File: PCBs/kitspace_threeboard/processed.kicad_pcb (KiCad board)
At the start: 2 copper layers, 58.2 x 49.3 mm, 52 parts, among them J1 USB_mini_micro_B, K1 KEYSW, K2 KEYSW, K3 KEYSW, SW1 SW_PUSH, U1 ATMEGA32U4, U2 24LC512, U3 24LC512, X1 XTAL_GND

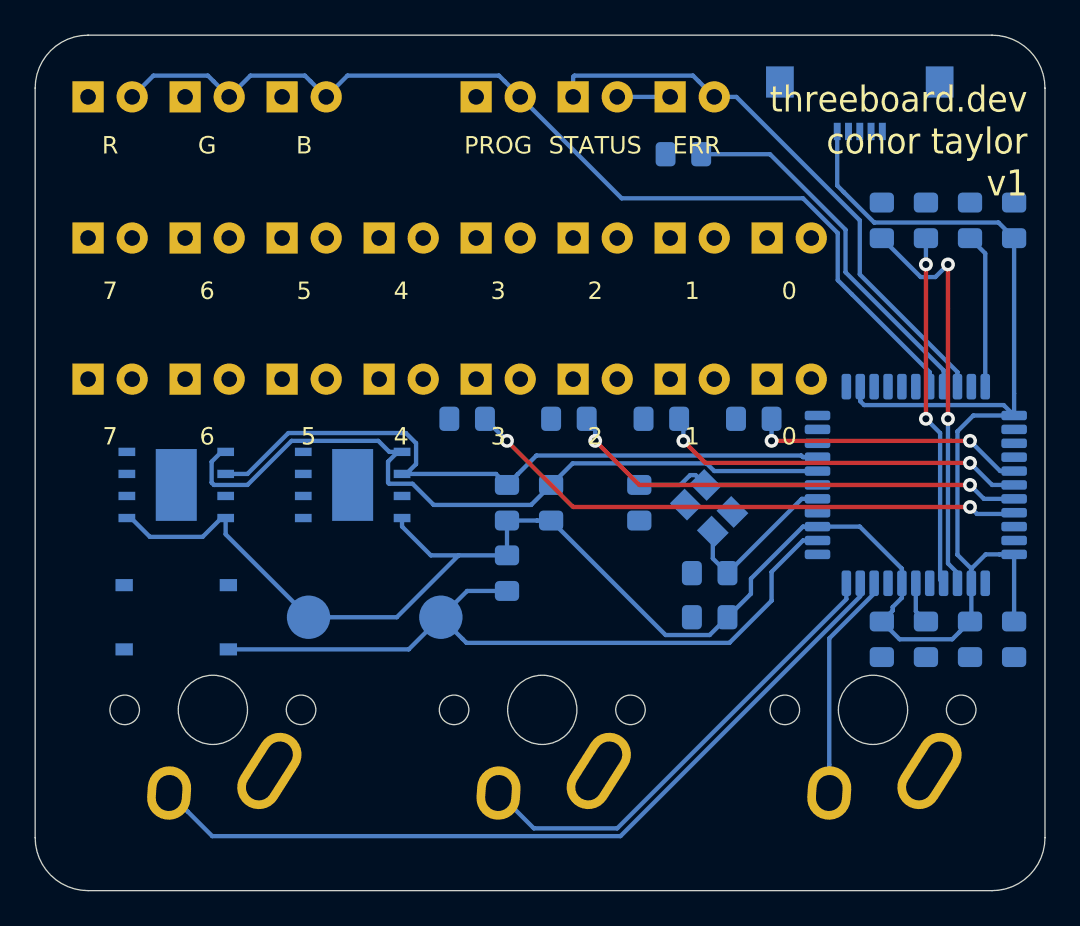
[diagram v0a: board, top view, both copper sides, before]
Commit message: recheck all circuits and clean up fill zone by rerouting the nets using freerouting and manually
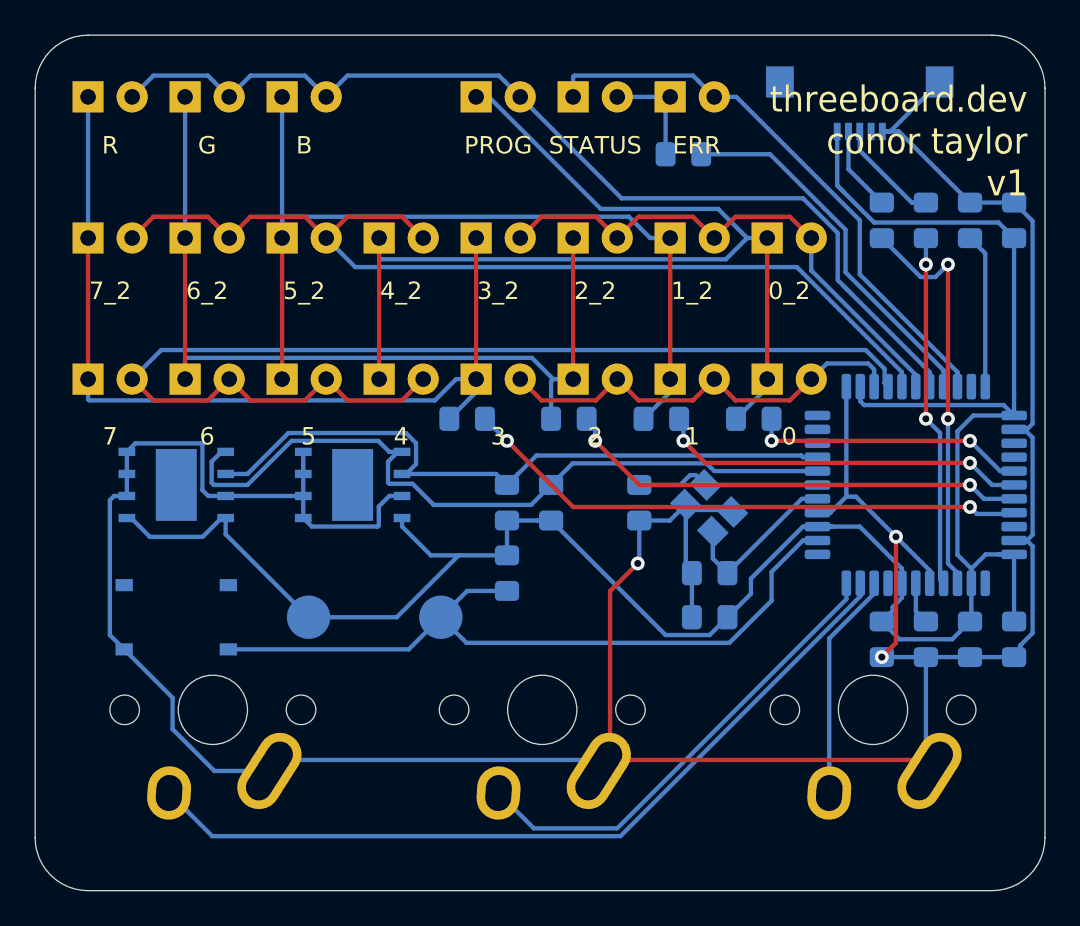
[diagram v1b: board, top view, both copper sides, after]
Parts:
- removed the REF** at (63.3, 59.5)
- added REF**_2: TestPoint_Pad_D2.5mm, TestPoint:TestPoint_Pad_D2.5mm, B.Cu at (63.3, 59.5)
- renumbered 0 to 0_2, 1 to 1_2, 2 to 2_2, 3 to 3_2, 4 to 4_2, 5 to 5_2, 6 to 6_2, 7 to 7_2
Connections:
- 0 pad 1: (no net) -> Net-(D12-Pad1)
- 0 pad 2: (no net) -> /row3
- 0_2 pad 1: (no net) -> Net-(D12-Pad1)
- 0_2 pad 2: (no net) -> /row1
- 1 pad 1: (no net) -> Net-(D11-Pad1)
- 1 pad 2: (no net) -> /row3
- 1_2 pad 1: (no net) -> Net-(D11-Pad1)
- 1_2 pad 2: (no net) -> /row1
- 2 pad 1: (no net) -> Net-(D10-Pad1)
- 2 pad 2: (no net) -> /row3
- 2_2 pad 1: (no net) -> Net-(D10-Pad1)
- 2_2 pad 2: (no net) -> /row1
- 3 pad 1: (no net) -> Net-(D1-Pad1)
- 3 pad 2: (no net) -> /row3
- 3_2 pad 1: (no net) -> Net-(D1-Pad1)
- 3_2 pad 2: (no net) -> /row1
- 4 pad 1: (no net) -> Net-(D12-Pad1)
- 4 pad 2: (no net) -> /row2
- 4_2 pad 1: (no net) -> Net-(D12-Pad1)
- 4_2 pad 2: (no net) -> /row0
- 5 pad 1: (no net) -> Net-(D11-Pad1)
- 5 pad 2: (no net) -> /row2
- 5_2 pad 1: (no net) -> Net-(D11-Pad1)
- 5_2 pad 2: (no net) -> /row0
- 6 pad 1: (no net) -> Net-(D10-Pad1)
- 6 pad 2: (no net) -> /row2
- 6_2 pad 1: (no net) -> Net-(D10-Pad1)
- 6_2 pad 2: (no net) -> /row0
- 7 pad 1: (no net) -> Net-(D1-Pad1)
- 7 pad 2: (no net) -> /row2
- 7_2 pad 1: (no net) -> Net-(D1-Pad1)
- 7_2 pad 2: (no net) -> /row0
- B pad 1: (no net) -> Net-(D11-Pad1)
- C1 pad 2: (no net) -> GND
- C2 pad 2: (no net) -> GND
- C3 pad 2: (no net) -> GND
- C4 pad 2: (no net) -> GND
- C5 pad 2: (no net) -> GND
- C6 pad 2: (no net) -> GND
- C7 pad 2: (no net) -> GND
- C8 pad 2: (no net) -> GND
- G pad 1: (no net) -> Net-(D10-Pad1)
- J1 pad 2: (no net) -> Net-(J1-Pad2)
- J1 pad 3: (no net) -> Net-(J1-Pad3)
- J1 pad 4: (no net) -> Net-(J1-Pad4)
- J1 pad 5: (no net) -> GND
- J1 pad 6: (no net) -> GND
- K1 pad 1: (no net) -> GND
- K2 pad 1: (no net) -> GND
- K3 pad 1: (no net) -> GND
- PROG pad 1: (no net) -> Net-(D12-Pad1)
- R pad 1: (no net) -> Net-(D1-Pad1)
- R2 pad 1: (no net) -> GND
- R3 pad 2: (no net) -> Net-(J1-Pad2)
- R4 pad 2: (no net) -> Net-(J1-Pad3)
- R5 pad 1: (no net) -> Net-(D1-Pad1)
- R6 pad 1: (no net) -> Net-(D10-Pad1)
- R7 pad 1: (no net) -> Net-(D11-Pad1)
- R8 pad 1: (no net) -> Net-(D12-Pad1)
- R9 pad 1: (no net) -> Net-(D21-Pad2)
- SW1 pad 1: (no net) -> GND
- U1 pad 1: (no net) -> Net-(U1-Pad1)
- U1 pad 12: (no net) -> Net-(U1-Pad12)
- U1 pad 15: (no net) -> GND
- U1 pad 20: (no net) -> Net-(U1-Pad20)
- U1 pad 21: (no net) -> Net-(U1-Pad21)
- U1 pad 22: (no net) -> Net-(U1-Pad22)
- U1 pad 23: (no net) -> GND
- U1 pad 25: (no net) -> /row3
- U1 pad 26: (no net) -> /row2
- U1 pad 27: (no net) -> /row0
- U1 pad 28: (no net) -> /row1
- U1 pad 32: (no net) -> Net-(U1-Pad32)
- U1 pad 35: (no net) -> GND
- U1 pad 36: (no net) -> Net-(U1-Pad36)
- U1 pad 37: (no net) -> Net-(U1-Pad37)
- U1 pad 42: (no net) -> Net-(U1-Pad42)
- U1 pad 43: (no net) -> GND
- U1 pad 5: (no net) -> GND
- U1 pad 8: (no net) -> Net-(U1-Pad8)
- U2 pad 2: (no net) -> GND
- U2 pad 3: (no net) -> GND
- U2 pad 4: (no net) -> GND
- U2 pad 7: (no net) -> GND
- U3 pad 1: (no net) -> GND
- U3 pad 2: (no net) -> GND
- U3 pad 3: (no net) -> GND
- U3 pad 4: (no net) -> GND
- U3 pad 7: (no net) -> GND
- X1 pad 3: (no net) -> GND
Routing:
- net GND: track 0.00 -> 197.4 mm, vias 0 -> 3
- net /row2: track 0.00 -> 65.4 mm
- net Net-(D12-Pad1): track 0.00 -> 63.1 mm
- net /row0: track 0.00 -> 57.0 mm
- net Net-(D1-Pad1): track 0.00 -> 51.7 mm
- net Net-(D11-Pad1): track 0.00 -> 51.7 mm
- net Net-(D10-Pad1): track 0.00 -> 50.8 mm
- net /row1: track 0.00 -> 31.3 mm
- net /row3: track 0.00 -> 24.9 mm
- net Net-(J1-Pad3): track 0.00 -> 5.80 mm
- net Net-(J1-Pad2): track 0.00 -> 4.54 mm
- net Net-(D21-Pad2): track 3.05 -> 6.09 mm
- net VCC: track 129.1 -> 130.4 mm
- net /row4: track 58.0 -> 58.7 mm
